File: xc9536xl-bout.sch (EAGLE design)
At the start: 2 parts

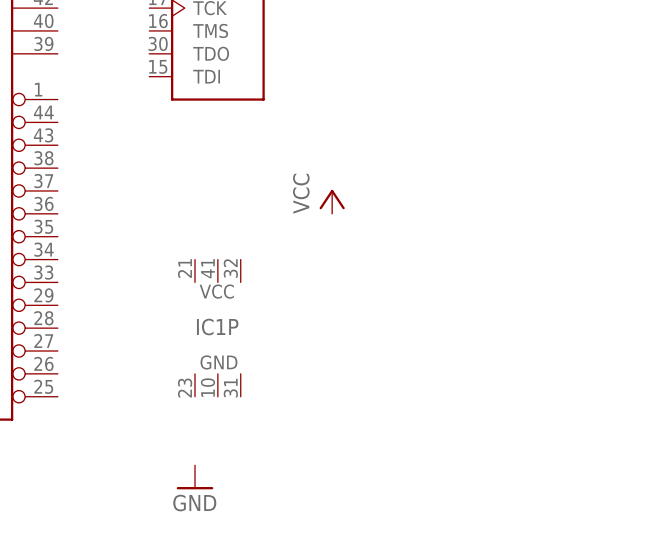
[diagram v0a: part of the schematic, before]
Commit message: Added decoupling capacitors for Xilinx supply pins
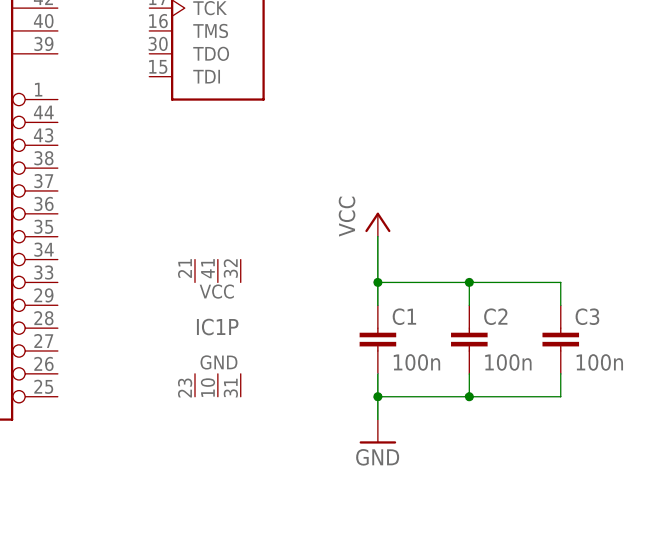
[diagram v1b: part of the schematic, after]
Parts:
- added C1, C2, C3: 100n, rcl:C-EU050-025X075
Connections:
- new net GND: C1.2, C2.2, C3.2
- new net VCC: C1.1, C2.1, C3.1
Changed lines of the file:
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@@
 <part name="GND1" library="supply1" library_urn="urn:adsk.eagle:library:371" deviceset="GND" device=""/>
 <part name="P+1" library="supply1" library_urn="urn:adsk.eagle:library:371" deviceset="VCC" device=""/>
+<part name="C1" library="rcl" library_urn="urn:adsk.eagle:library:334" deviceset="C-EU" device="050-025X075" package3d_urn="urn:adsk.eagle:package:23637/1" value="100n"/>
+<part name="C2" library="rcl" library_urn="urn:adsk.eagle:library:334" deviceset="C-EU" device="050-025X075" package3d_urn="urn:adsk.eagle:package:23637/1" value="100n"/>
+<part name="C3" library="rcl" library_urn="urn:adsk.eagle:library:334" deviceset="C-EU" device="050-025X075" package3d_urn="urn:adsk.eagle:package:23637/1" value="100n"/>
 </parts>
 <sheets>
@@
 <attribute name="NAME" x="177.8" y="100.838" size="1.778" layer="95"/>
 </instance>
-<instance part="GND1" gate="1" x="177.8" y="83.82" smashed="yes">
-<attribute name="VALUE" x="175.26" y="81.28" size="1.778" layer="96"/>
+<instance part="GND1" gate="1" x="198.12" y="88.9" smashed="yes">
+<attribute name="VALUE" x="195.58" y="86.36" size="1.778" layer="96"/>
 </instance>
-<instance part="P+1" gate="VCC" x="193.04" y="116.84" smashed="yes">
-<attribute name="VALUE" x="190.5" y="114.3" size="1.778" layer="96" rot="R90"/>
+<instance part="P+1" gate="VCC" x="198.12" y="114.3" smashed="yes">
+<attribute name="VALUE" x="195.58" y="111.76" size="1.778" layer="96" rot="R90"/>
+</instance>
+<instance part="C1" gate="G$1" x="198.12" y="101.6" smashed="yes">
+<attribute name="NAME" x="199.644" y="101.981" size="1.778" layer="95"/>
+<attribute name="VALUE" x="199.644" y="96.901" size="1.778" layer="96"/>
+</instance>
+<instance part="C2" gate="G$1" x="208.28" y="101.6" smashed="yes">
+<attribute name="NAME" x="209.804" y="101.981" size="1.778" layer="95"/>
+<attribute name="VALUE" x="209.804" y="96.901" size="1.778" layer="96"/>
+</instance>
+<instance part="C3" gate="G$1" x="218.44" y="101.6" smashed="yes">
+<attribute name="NAME" x="219.964" y="101.981" size="1.778" layer="95"/>
+<attribute name="VALUE" x="219.964" y="96.901" size="1.778" layer="96"/>
 </instance>
 </instances>
@@
 </busses>
 <nets>
+<net name="VCC" class="0">
+<segment>
+<pinref part="P+1" gate="VCC" pin="VCC"/>
+<pinref part="C1" gate="G$1" pin="1"/>
+<wire x1="198.12" y1="111.76" x2="198.12" y2="106.68" width="0.1524" layer="91"/>
+<pinref part="C2" gate="G$1" pin="1"/>
+<wire x1="198.12" y1="106.68" x2="198.12" y2="104.14" width="0.1524" layer="91"/>
+<wire x1="208.28" y1="104.14" x2="208.28" y2="106.68" width="0.1524" layer="91"/>
+<wire x1="208.28" y1="106.68" x2="198.12" y2="106.68" width="0.1524" layer="91"/>
+<junction x="198.12" y="106.68"/>
+<pinref part="C3" gate="G$1" pin="1"/>
+<wire x1="208.28" y1="106.68" x2="218.44" y2="106.68" width="0.1524" layer="91"/>
+<wire x1="218.44" y1="106.68" x2="218.44" y2="104.14" width="0.1524" layer="91"/>
+<junction x="208.28" y="106.68"/>
+</segment>
+</net>
+<net name="GND" class="0">
+<segment>
+<pinref part="GND1" gate="1" pin="GND"/>
+<pinref part="C1" gate="G$1" pin="2"/>
+<wire x1="198.12" y1="91.44" x2="198.12" y2="93.98" width="0.1524" layer="91"/>
+<pinref part="C2" gate="G$1" pin="2"/>
+<wire x1="198.12" y1="93.98" x2="198.12" y2="96.52" width="0.1524" layer="91"/>
+<wire x1="198.12" y1="93.98" x2="208.28" y2="93.98" width="0.1524" layer="91"/>
+<wire x1="208.28" y1="93.98" x2="208.28" y2="96.52" width="0.1524" layer="91"/>
+<junction x="198.12" y="93.98"/>
+<pinref part="C3" gate="G$1" pin="2"/>
+<wire x1="208.28" y1="93.98" x2="218.44" y2="93.98" width="0.1524" layer="91"/>
+<wire x1="218.44" y1="93.98" x2="218.44" y2="96.52" width="0.1524" layer="91"/>
+<junction x="208.28" y="93.98"/>
+</segment>
+</net>
 </nets>
 </sheet>
@@
 packages will not be understood (or retained) with this version.
 </note>
+<note version="8.4" severity="warning">
+Since Version 8.4, EAGLE supports properties for SPICE simulation.
+Probes in schematics and SPICE mapping objects found in parts and library devices
+will not be understood with this version. Update EAGLE to the latest version
+for full support of SPICE simulation.
+</note>
 </compatibility>

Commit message: Voltage drop diodes and few signals for tests
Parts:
- added D1, D2: 1N4004, diode:1N4004
- added JP1, JP2: (no value), jumper:JP1E
- added LED1: (no value), led:LED5MM
- added R1: (no value), rcl:R-EU_0207/10
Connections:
- new net FB1MC1: IC1G.FB1MC1, SV2.2
- new net FB1MC2: IC1G.FB1MC2, SV2.3
- new net FB2MC1: IC1G.FB2MC1, SV2.1
- new net N$1: D1.C, D2.A, JP1.1, JP2.2
- new net N$2: LED1.A, R1.1
- new net VBAT_4V5: D1.A, JP1.2, SV2.40
- net GND: now also LED1.C, SV2.39
- net VCC: now also D2.C, JP2.1, R1.2
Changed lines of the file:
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@@
 <layer number="97" name="Info" color="7" fill="1" visible="yes" active="yes"/>
 <layer number="98" name="Guide" color="6" fill="1" visible="yes" active="yes"/>
+<layer number="99" name="SpiceOrder" color="5" fill="1" visible="yes" active="yes"/>
 <layer number="250" name="Descript" color="3" fill="1" visible="no" active="no"/>
 <layer number="251" name="SMDround" color="4" fill="9" visible="no" active="yes"/>
@@
 <part name="C2" library="rcl" library_urn="urn:adsk.eagle:library:334" deviceset="C-EU" device="050-025X075" package3d_urn="urn:adsk.eagle:package:23637/1" value="100n"/>
 <part name="C3" library="rcl" library_urn="urn:adsk.eagle:library:334" deviceset="C-EU" device="050-025X075" package3d_urn="urn:adsk.eagle:package:23637/1" value="100n"/>
+<part name="D1" library="diode" library_urn="urn:adsk.eagle:library:210" deviceset="1N4004" device="" package3d_urn="urn:adsk.eagle:package:43336/1"/>
+<part name="D2" library="diode" library_urn="urn:adsk.eagle:library:210" deviceset="1N4004" device="" package3d_urn="urn:adsk.eagle:package:43336/1"/>
+<part name="P+2" library="supply1" library_urn="urn:adsk.eagle:library:371" deviceset="VCC" device=""/>
+<part name="JP1" library="jumper" library_urn="urn:adsk.eagle:library:252" deviceset="JP1E" device="" package3d_urn="urn:adsk.eagle:package:15455/1"/>
+<part name="JP2" library="jumper" library_urn="urn:adsk.eagle:library:252" deviceset="JP1E" device="" package3d_urn="urn:adsk.eagle:package:15455/1"/>
+<part name="R1" library="rcl" library_urn="urn:adsk.eagle:library:334" deviceset="R-EU_" device="0207/10" package3d_urn="urn:adsk.eagle:package:23491/1"/>
+<part name="LED1" library="led" library_urn="urn:adsk.eagle:library:259" deviceset="LED" device="5MM" package3d_urn="urn:adsk.eagle:package:15799/2"/>
+<part name="GND2" library="supply1" library_urn="urn:adsk.eagle:library:371" deviceset="GND" device=""/>
+<part name="GND3" library="supply1" library_urn="urn:adsk.eagle:library:371" deviceset="GND" device=""/>
+<part name="GND4" library="supply1" library_urn="urn:adsk.eagle:library:371" deviceset="GND" device=""/>
 </parts>
 <sheets>
@@
 <attribute name="NAME" x="219.964" y="101.981" size="1.778" layer="95"/>
 <attribute name="VALUE" x="219.964" y="96.901" size="1.778" layer="96"/>
+</instance>
+<instance part="D1" gate="1" x="45.72" y="162.56" smashed="yes" rot="R180">
+<attribute name="NAME" x="43.18" y="162.0774" size="1.778" layer="95" rot="R180"/>
+<attribute name="VALUE" x="48.26" y="159.7914" size="1.778" layer="96" rot="R180"/>
+</instance>
+<instance part="D2" gate="1" x="22.86" y="162.56" smashed="yes" rot="R180">
+<attribute name="NAME" x="20.32" y="162.0774" size="1.778" layer="95" rot="R180"/>
+<attribute name="VALUE" x="25.4" y="159.7914" size="1.778" layer="96" rot="R180"/>
+</instance>
+<instance part="P+2" gate="VCC" x="10.16" y="172.72" smashed="yes">
+<attribute name="VALUE" x="7.62" y="170.18" size="1.778" layer="96" rot="R90"/>
+</instance>
+<instance part="JP1" gate="A" x="43.18" y="170.18" smashed="yes">
+<attribute name="NAME" x="41.91" y="170.18" size="1.778" layer="95" rot="R90"/>
+<attribute name="VALUE" x="48.895" y="170.18" size="1.778" layer="96" rot="R90"/>
+</instance>
+<instance part="JP2" gate="A" x="22.86" y="170.18" smashed="yes">
+<attribute name="NAME" x="21.59" y="170.18" size="1.778" layer="95" rot="R90"/>
+<attribute name="VALUE" x="28.575" y="170.18" size="1.778" layer="96" rot="R90"/>
+</instance>
+<instance part="R1" gate="G$1" x="10.16" y="149.86" smashed="yes" rot="R90">
+<attribute name="NAME" x="8.6614" y="146.05" size="1.778" layer="95" rot="R90"/>
+<attribute name="VALUE" x="13.462" y="146.05" size="1.778" layer="96" rot="R90"/>
+</instance>
+<instance part="LED1" gate="G$1" x="10.16" y="137.16" smashed="yes">
+<attribute name="NAME" x="13.716" y="132.588" size="1.778" layer="95" rot="R90"/>
+<attribute name="VALUE" x="15.875" y="132.588" size="1.778" layer="96" rot="R90"/>
+</instance>
+<instance part="GND2" gate="1" x="73.66" y="96.52" smashed="yes">
+<attribute name="VALUE" x="71.12" y="93.98" size="1.778" layer="96"/>
+</instance>
+<instance part="GND3" gate="1" x="10.16" y="124.46" smashed="yes">
+<attribute name="VALUE" x="7.62" y="121.92" size="1.778" layer="96"/>
+</instance>
+<instance part="GND4" gate="1" x="91.44" y="160.02" smashed="yes">
+<attribute name="VALUE" x="88.9" y="157.48" size="1.778" layer="96"/>
 </instance>
 </instances>
@@
 <junction x="208.28" y="106.68"/>
 </segment>
+<segment>
+<pinref part="P+2" gate="VCC" pin="VCC"/>
+<wire x1="20.32" y1="162.56" x2="10.16" y2="162.56" width="0.1524" layer="91"/>
+<wire x1="10.16" y1="162.56" x2="10.16" y2="167.64" width="0.1524" layer="91"/>
+<pinref part="JP2" gate="A" pin="1"/>
+<wire x1="10.16" y1="167.64" x2="10.16" y2="170.18" width="0.1524" layer="91"/>
+<wire x1="22.86" y1="167.64" x2="10.16" y2="167.64" width="0.1524" layer="91"/>
+<junction x="10.16" y="167.64"/>
+<pinref part="D2" gate="1" pin="C"/>
+<pinref part="R1" gate="G$1" pin="2"/>
+<wire x1="10.16" y1="162.56" x2="10.16" y2="154.94" width="0.1524" layer="91"/>
+<junction x="10.16" y="162.56"/>
+</segment>
 </net>
 <net name="GND" class="0">
@@
 <junction x="208.28" y="93.98"/>
 </segment>
-</net>
+<segment>
+<pinref part="LED1" gate="G$1" pin="C"/>
+<pinref part="GND3" gate="1" pin="GND"/>
+<wire x1="10.16" y1="132.08" x2="10.16" y2="127" width="0.1524" layer="91"/>
+</segment>
+<segment>
+<pinref part="SV2" gate="1" pin="39"/>
+<pinref part="GND4" gate="1" pin="GND"/>
+<wire x1="78.74" y1="162.56" x2="91.44" y2="162.56" width="0.1524" layer="91"/>
+</segment>
+</net>
+<net name="N$1" class="0">
+<segment>
+<pinref part="D1" gate="1" pin="C"/>
+<pinref part="D2" gate="1" pin="A"/>
+<wire x1="43.18" y1="162.56" x2="35.56" y2="162.56" width="0.1524" layer="91"/>
+<pinref part="JP1" gate="A" pin="1"/>
+<wire x1="35.56" y1="162.56" x2="25.4" y2="162.56" width="0.1524" layer="91"/>
+<wire x1="43.18" y1="167.64" x2="35.56" y2="167.64" width="0.1524" layer="91"/>
+<wire x1="35.56" y1="167.64" x2="35.56" y2="162.56" width="0.1524" layer="91"/>
+<junction x="35.56" y="162.56"/>
+<pinref part="JP2" gate="A" pin="2"/>
+<wire x1="35.56" y1="167.64" x2="25.4" y2="167.64" width="0.1524" layer="91"/>
+<junction x="35.56" y="167.64"/>
+</segment>
+</net>
+<net name="VBAT_4V5" class="0">
+<segment>
+<pinref part="SV2" gate="1" pin="40"/>
+<pinref part="D1" gate="1" pin="A"/>
+<wire x1="63.5" y1="162.56" x2="48.26" y2="162.56" width="0.1524" layer="91"/>
+<label x="50.8" y="165.1" size="1.778" layer="95"/>
+<wire x1="48.26" y1="162.56" x2="48.26" y2="167.64" width="0.1524" layer="91"/>
+<junction x="48.26" y="162.56"/>
+<pinref part="JP1" gate="A" pin="2"/>
+<wire x1="48.26" y1="167.64" x2="45.72" y2="167.64" width="0.1524" layer="91"/>
+</segment>
+</net>
+<net name="N$2" class="0">
+<segment>
+<pinref part="R1" gate="G$1" pin="1"/>
+<pinref part="LED1" gate="G$1" pin="A"/>
+<wire x1="10.16" y1="144.78" x2="10.16" y2="139.7" width="0.1524" layer="91"/>
+</segment>
+</net>
+<net name="FB2MC1" class="0">
+<segment>
+<pinref part="IC1" gate="G" pin="FB2MC1"/>
+<wire x1="162.56" y1="127" x2="167.64" y2="127" width="0.1524" layer="91"/>
+<wire x1="167.64" y1="127" x2="167.64" y2="144.78" width="0.1524" layer="91"/>
+<wire x1="167.64" y1="144.78" x2="99.06" y2="144.78" width="0.1524" layer="91"/>
+<wire x1="99.06" y1="144.78" x2="99.06" y2="114.3" width="0.1524" layer="91"/>
+<pinref part="SV2" gate="1" pin="1"/>
+<wire x1="99.06" y1="114.3" x2="78.74" y2="114.3" width="0.1524" layer="91"/>
+<label x="81.28" y="111.76" size="1.778" layer="95"/>
+</segment>
+</net>
+<net name="FB1MC1" class="0">
+<segment>
+<pinref part="SV2" gate="1" pin="2"/>
+<wire x1="63.5" y1="114.3" x2="60.96" y2="114.3" width="0.1524" layer="91"/>
+<wire x1="60.96" y1="114.3" x2="60.96" y2="109.22" width="0.1524" layer="91"/>
+<wire x1="60.96" y1="109.22" x2="109.22" y2="109.22" width="0.1524" layer="91"/>
+<wire x1="109.22" y1="109.22" x2="109.22" y2="127" width="0.1524" layer="91"/>
+<pinref part="IC1" gate="G" pin="FB1MC1"/>
+<wire x1="109.22" y1="127" x2="124.46" y2="127" width="0.1524" layer="91"/>
+<label x="63.5" y="106.68" size="1.778" layer="95"/>
+</segment>
+</net>
+<net name="FB1MC2" class="0">
+<segment>
+<pinref part="IC1" gate="G" pin="FB1MC2"/>
+<wire x1="124.46" y1="124.46" x2="96.52" y2="124.46" width="0.1524" layer="91"/>
+<wire x1="96.52" y1="124.46" x2="96.52" y2="116.84" width="0.1524" layer="91"/>
+<pinref part="SV2" gate="1" pin="3"/>
+<wire x1="96.52" y1="116.84" x2="78.74" y2="116.84" width="0.1524" layer="91"/>
+<label x="81.28" y="116.84" size="1.778" layer="95"/>
+</segment>
+</net>
